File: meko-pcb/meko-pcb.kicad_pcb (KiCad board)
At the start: 4 copper layers, 37 x 69 mm, 165 parts, among them IC1 AS5600-ASOM, IC2 TCAL9538RSVR, IC3 LP5912-3.3DRVR, IC4 ES9218PQ, IC5 BQ27427YZFR, J1 GDEY0154D67, J2 MEM2090-00-145-00-A, J3 USB_C_Receptacle_USB2.0_16P, J4 SJ2-35954B-SMT-TR, M1 HD-EMB1204-SM, Q1 SS8050, Q2 SS8050, Q3 SS8050, Q4 Si1308EDL, SW1 SW_Push, SW2 SW_Push, SW3 SW_Push, SW4 SW_Push, SW5 SW_Push, SW6 SW_Push, SW7 SW_Push, U1 ESP32-PICO-MINI-02, U10 LP5907SNX-1.8/NOPB, U2 BQ24075RGT, U3 LP5907SNX-3.3/NOPB, U4 LP5907SNX-3.3/NOPB, U6 LP5907SNX-3.3/NOPB, U7 LP5907SNX-1.8/NOPB, U8 USBLC6-2SC6, U9 CP2102N-Axx-xQFN24, Y1 ECS-2520SMV-500-GP-TR

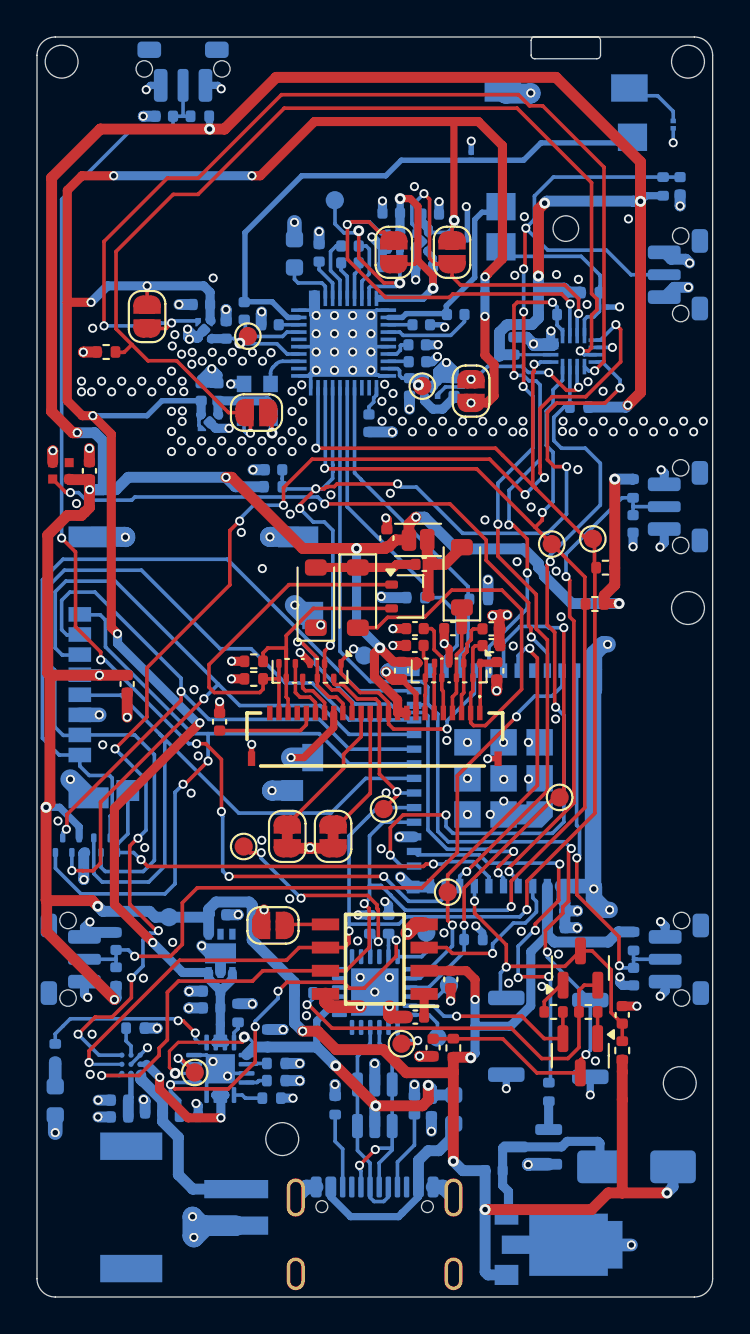
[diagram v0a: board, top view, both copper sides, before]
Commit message: removed seperate pcb file, you can undround the tracks easily
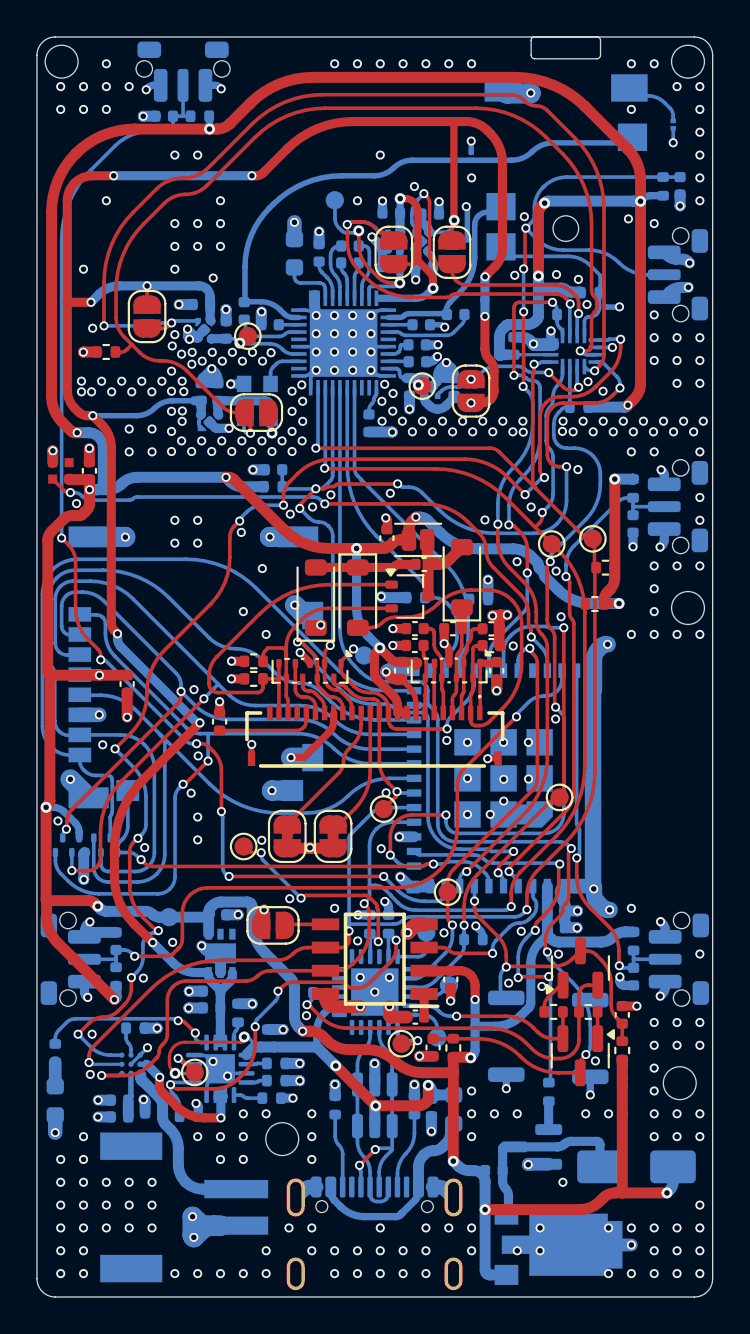
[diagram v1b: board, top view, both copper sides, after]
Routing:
- net +3V3: track 283.7 -> 278.5 mm
- net GND: track 192.5 -> 188.2 mm, vias 281 -> 455
- net /PWR_FUEL_GPOUT: track 71.0 -> 68.1 mm
- net REG-OUT: track 131.2 -> 128.3 mm
- net /I2C_SCL: track 88.6 -> 86.6 mm
- net /AUDIO_DATA_CLK/BOOT: track 60.3 -> 58.4 mm
- net /AUDIO_MLCK_EN: track 58.6 -> 56.8 mm
- net /BTN_VOL_UP: track 59.3 -> 57.9 mm
- net /MEM_DAT0: track 47.6 -> 46.2 mm
- net /PWR_EN3V3VCCA: track 55.8 -> 54.6 mm
- net /AUDIO_DISPL_RESETB: track 52.2 -> 51.2 mm
- net /I2C_SDA: track 89.4 -> 88.4 mm
- net /BTN_PWR: track 65.7 -> 64.7 mm
- net /MEM_DAT1: track 40.9 -> 39.9 mm
- net /MEM_CLK: track 35.5 -> 34.5 mm
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
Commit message: small changes, readme updates
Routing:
- net GND: vias 455 -> 540

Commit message: continued work om nrf53
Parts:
- removed C23, C25, C26: 4.7uF, Capacitor_SMD:C_0402_1005Metric
- removed C57, C58: 1uF, Capacitor_SMD:C_0402_1005Metric
- removed D14: LED, LED_SMD:LED_0603_1608Metric
- removed IC2: TCAL9538RSVR, TCAL9538RSVR:QFN40P180X260X55-16N
- removed IC5: BQ27427YZFR, BQ27427YZFR:BGA9C50P3X3_158X162X62
- removed Q1, Q2: SS8050, Package_TO_SOT_SMD:SOT-23
- removed R1, R14, R15, R16, R18, R2, R21, R22, R23, R24, R3, R31, R4, R5, R6, R7, R8: 10k, Resistor_SMD:R_0402_1005Metric
- removed R17: 47k, Resistor_SMD:R_0402_1005Metric
- removed R19, R32: 1.5k, Resistor_SMD:R_0402_1005Metric
- removed R20: 1.8k, Resistor_SMD:R_0402_1005Metric
- removed R30: 100k, Resistor_SMD:R_0402_1005Metric
- removed SW7: SW_Push, Button_Switch_SMD:SW_Push_SPST_NO_Alps_SKRK
- removed TP1, TP10, TP2, TP3, TP4, TP5, TP6, TP7: TestPoint, TestPoint:TestPoint_Pad_D1.0mm
- removed U8: USBLC6-2SC6, Package_TO_SOT_SMD:SOT-23-6
- removed U9: CP2102N-Axx-xQFN24, Package_DFN_QFN:QFN-24-1EP_4x4mm_P0.5mm_EP2.6x2.6mm
- added C31: 12pF, Capacitor_SMD:C_0402_1005Metric, F.Cu at (48.8, 71.0)
- added C32: 12pF, Capacitor_SMD:C_0402_1005Metric, F.Cu at (48.8, 73.0)
- added C35: 100nF, Capacitor_SMD:C_0402_1005Metric, F.Cu at (48.8, 75.0)
- added C37: 100nF, Capacitor_SMD:C_0402_1005Metric, F.Cu at (48.8, 77.0)
- added C39: 100nF, Capacitor_SMD:C_0402_1005Metric, F.Cu at (51.7, 67.1)
- added C59: 100nF, Capacitor_SMD:C_0402_1005Metric, F.Cu at (51.7, 71.0)
- added C62: 100nF, Capacitor_SMD:C_0402_1005Metric, F.Cu at (51.7, 77.0)
- added C63: 100nF, Capacitor_SMD:C_0402_1005Metric, F.Cu at (54.5, 67.1)
- added C64: 100nF, Capacitor_SMD:C_0402_1005Metric, F.Cu at (54.5, 69.1)
- added C65: 0.7pF, Capacitor_SMD:C_0402_1005Metric, F.Cu at (54.5, 71.0)
- added C66: N.C., Capacitor_SMD:C_0402_1005Metric, F.Cu at (54.5, 73.0)
- added C67: 2.2nF, Capacitor_SMD:C_0402_1005Metric, F.Cu at (54.5, 75.0)
- added C68: 1uF, Capacitor_SMD:C_0402_1005Metric, F.Cu at (54.5, 77.0)
- added C69: 1uF, Capacitor_SMD:C_0402_1005Metric, F.Cu at (57.4, 67.1)
- added C70: 100nF, Capacitor_SMD:C_0402_1005Metric, F.Cu at (57.4, 69.1)
- added C71: 4.7uF, Capacitor_SMD:C_0402_1005Metric, F.Cu at (57.4, 71.0)
- added C72: 4.7uF, Capacitor_SMD:C_0402_1005Metric, F.Cu at (57.4, 73.0)
- added Y2: 32MHz, Crystal:Crystal_SMD_2520-4Pin_2.5x2.0mm, F.Cu at (61.3, 61.5)
- added Y4: 32.768 kHz, Crystal:Crystal_SMD_3215-2Pin_3.2x1.5mm, F.Cu at (61.6, 57.8)
- C15: value 1uF -> 12pF; moved to F.Cu
- C40, C61, F1, R25, R26: moved to F.Cu
- C6: value 100nF -> 12pF
- C60: value 4.7uF -> 100nF; moved to F.Cu
- U1: value ESP32-PICO-MINI-02 -> nRF5340-QKxx; footprint PCM_Espressif:ESP32-PICO-MINI-02 -> Package_DFN_QFN:Nordic_AQFN-94-1EP_7x7mm_P0.4mm
- U2: value BQ24075RGT -> TP4056-42-ESOP8; footprint Package_DFN_QFN:VQFN-16-1EP_3x3mm_P0.5mm_EP1.6x1.6mm -> Package_SO:SOIC-8-1EP_3.9x4.9mm_P1.27mm_EP2.41x3.3mm_ThermalVias
- moved C15 59.4 mm to (48.8, 69.1), turned to 0 degrees
- moved C6 57.3 mm to (48.8, 67.1), turned to 0 degrees
- moved U1 54.6 mm to (51.7, 89.3), turned to 180 degrees
- moved C61 50.6 mm to (51.7, 75.0)
- moved C60 50.3 mm to (51.7, 73.0), turned to 0 degrees
- moved C40 44.8 mm to (51.7, 69.1), turned to 0 degrees
- moved F1 38.5 mm to (61.0, 64.8), turned to 0 degrees
- moved R26 34.0 mm to (65.0, 62.5), turned to 0 degrees
- moved R25 31.5 mm to (65.0, 60.5), turned to 0 degrees
- moved U2 18.9 mm to (64.8, 80.6), turned to -90 degrees
- moved J3 0.17 mm to (92.2, 88.2)
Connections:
- net /USB/CC1 renamed /CC1
- net /USB/CC2 renamed /CC2
- C15 pad 1: GND -> /XC1
- C15 pad 2: +3V3 -> GND
- C6 pad 1: /ESP_EN -> /XL2
- C60 pad 1: GND -> Net-(C35-Pad1)
- C60 pad 2: +3V3 -> GND
- C61 pad 1: +3V3 -> Net-(C35-Pad1)
- C7 pad 1: /AUDIO_DATA_CLK/BOOT -> unconnected-(C7-Pad1)
- J3 pad A6: /USB/D+ -> /D+
- J3 pad A7: /USB/D- -> /D-
- J3 pad B6: /USB/D+ -> /D+
- J3 pad B7: /USB/D- -> /D-
- U2 pad 1: /power/TS -> unconnected-(U2-TEMP-Pad1)
- U2 pad 2: /power/SRX -> unconnected-(U2-PROG-Pad2)
- U2 pad 3: /power/SRX -> unconnected-(U2-GND-Pad3)
- U2 pad 4: GND -> unconnected-(U2-V_{CC}-Pad4)
- U2 pad 5: /PWR_EN_USB -> unconnected-(U2-BAT-Pad5)
- U2 pad 6: +5V -> unconnected-(U2-~{STDBY}-Pad6)
- U2 pad 7: Net-(U2-~{PGOOD}) -> unconnected-(U2-~{CHRG}-Pad7)
- U2 pad 8: GND -> unconnected-(U2-CE-Pad8)
- U2 pad 9: Net-(U2-~{CHG}) -> unconnected-(U2-EPAD-Pad9)
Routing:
- net (no net): track 0.00 -> 300.5 mm, vias 0 -> 37
- net /PWR_FUEL_GPOUT: track 68.1 -> 0.00 mm, vias 10 -> 0
- net /EXP_~{INT}: track 41.9 -> 0.00 mm, vias 4 -> 0
- net /RXD: track 28.8 -> 0.00 mm, vias 2 -> 0
- net /EXP_~{RES}: track 26.9 -> 0.00 mm, vias 4 -> 0
- net /TXD: track 23.0 -> 0.00 mm, vias 2 -> 0
- net /PWR_EN_USB: track 22.8 -> 0.00 mm, vias 4 -> 0
- net /~{RST}: track 22.4 -> 0.00 mm, vias 1 -> 0
- net /USB/~{SUSP}: track 12.8 -> 0.00 mm, vias 3 -> 0
- net /USB/D+: track 12.5 -> 0.00 mm, vias 2 -> 0
- net /D+: track 0.00 -> 12.5 mm, vias 0 -> 2
- net /USB/D-: track 11.3 -> 0.00 mm
- net /D-: track 0.00 -> 11.3 mm
- net /~{DTR}: track 10.4 -> 0.00 mm, vias 1 -> 0
- net Net-(U2-~{CHG}): track 9.79 -> 0.00 mm, vias 2 -> 0
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
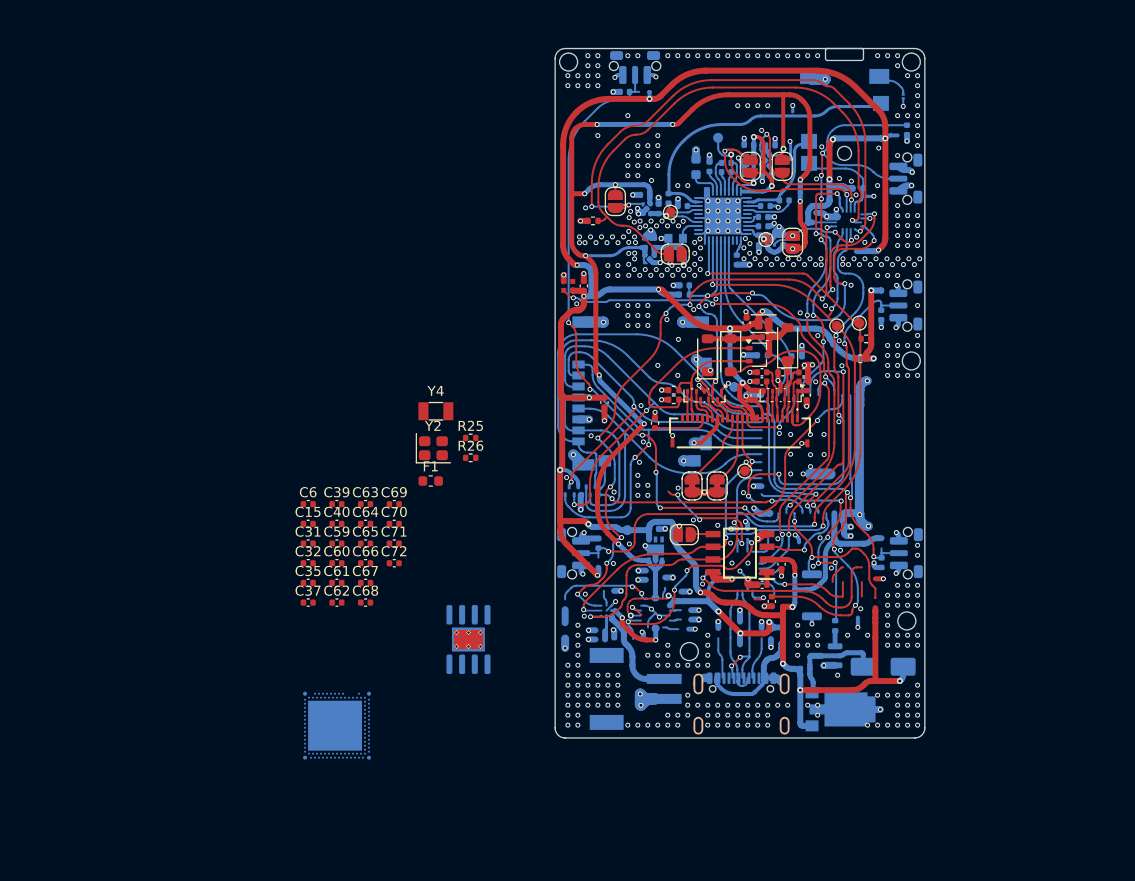
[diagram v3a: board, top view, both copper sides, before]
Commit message: added new ldos, made improvements to the schematic
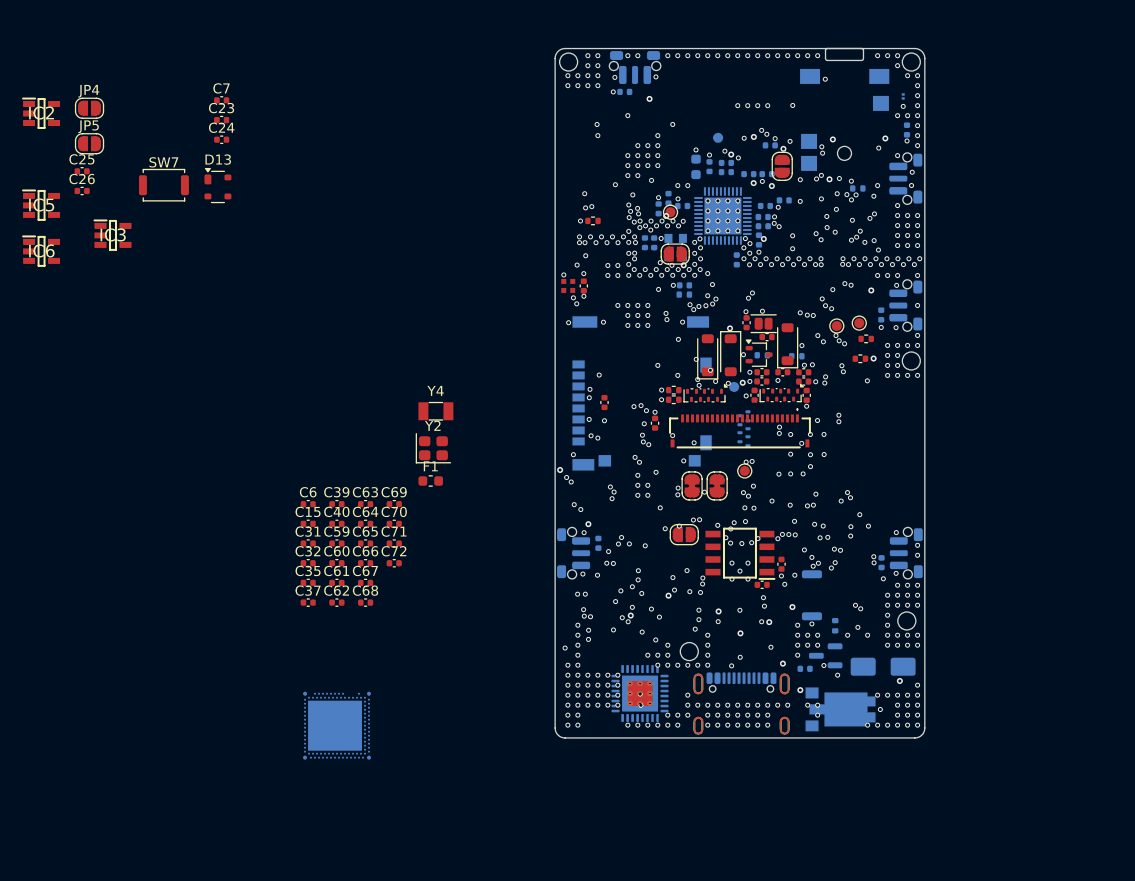
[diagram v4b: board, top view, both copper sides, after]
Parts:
- removed BT1: Battery_Cell, S2B-PH-SM4-TB_LF__SN_:JST_S2B-PH-SM4-TB_LF__SN_
- removed C29, C36, C38: 1uF, Capacitor_SMD:C_0402_1005Metric
- removed C33: 4.7uF, Capacitor_SMD:C_0402_1005Metric
- removed D10, D11, D12: D_TVS, CD0201-T2.0LC:CD0201T20LC
- removed JP10, JP6, JP8: SolderJumper_2_Open, Jumper:SolderJumper-2_P1.3mm_Open_RoundedPad1.0x1.5mm
- removed R25, R26: 5.1k, Resistor_SMD:R_0402_1005Metric
- removed TP17, TP18: TestPoint, TestPoint:TestPoint_Pad_D1.0mm
- removed U10, U7: LP5907SNX-1.8/NOPB, Package_SON:Texas_X2SON-4_1x1mm_P0.65mm
- removed U3, U4, U6: LP5907SNX-3.3/NOPB, Package_SON:Texas_X2SON-4_1x1mm_P0.65mm
- added C23: 10uF, Capacitor_SMD:C_0402_1005Metric, F.Cu at (40.1, 28.7)
- added C25: 1uF, Capacitor_SMD:C_0402_1005Metric, F.Cu at (26.2, 33.8)
- added C26: 1uF, Capacitor_SMD:C_0402_1005Metric, F.Cu at (26.2, 35.8)
- added D13: PRTR5V0U2X, Package_TO_SOT_SMD:SOT-143, F.Cu at (39.8, 35.4)
- added IC2: TPS7A2033PDBVR, TPS7A2018PDBVR:SOT95P280X145-5N, F.Cu at (22.1, 28.0)
- added IC5: TPS7A2018PDBVR, TPS7A2018PDBVR:SOT95P280X145-5N, F.Cu at (22.1, 37.2)
- added IC6: TPS7A2033PDBVR, TPS7A2018PDBVR:SOT95P280X145-5N, F.Cu at (22.1, 41.8)
- added JP4: SolderJumper_2_Open, Jumper:SolderJumper-2_P1.3mm_Open_RoundedPad1.0x1.5mm, F.Cu at (26.9, 27.5)
- added JP5: SolderJumper_2_Open, Jumper:SolderJumper-2_P1.3mm_Open_RoundedPad1.0x1.5mm, F.Cu at (26.9, 31.0)
- added SW7: SW_Push, Button_Switch_SMD:SW_Push_SPST_NO_Alps_SKRK, F.Cu at (34.4, 35.2)
- C24: moved to F.Cu
- C40: value 10uF -> 1uF
- C7: value 100nF -> 10uF
- IC3: value LP5912-3.3DRVR -> TPS7A2033PDBVR; footprint LP5912-3.3DRVR:SON65P200X200X80-7N -> TPS7A2018PDBVR:SOT95P280X145-5N; moved to F.Cu
- U2: value TP4056-42-ESOP8 -> nPM1300-QEXX; footprint Package_SO:SOIC-8-1EP_3.9x4.9mm_P1.27mm_EP2.41x3.3mm_ThermalVias -> Package_DFN_QFN:QFN-32-1EP_5x5mm_P0.5mm_EP3.6x3.6mm_ThermalVias
- moved C7 74.5 mm to (40.1, 26.7), turned to 0 degrees
- moved C24 63.7 mm to (40.1, 30.6)
- moved IC3 62.8 mm to (29.2, 40.2), turned to 0 degrees
- moved U2 18.0 mm to (82.0, 86.1), turned to 180 degrees
- moved D8 17.3 mm to (92.4, 59.6), turned to 180 degrees
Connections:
- C10 pad 1: +3V3 -> +HALL3V3
- C35 pad 1: Net-(C35-Pad1) -> +3V3
- C37 pad 1: Net-(C35-Pad1) -> +3V3
- C39 pad 1: Net-(C35-Pad1) -> +3V3
- C40 pad 1: +5V -> (no net)
- C49 pad 1: +3V3AVDD -> +3V3
- C59 pad 1: Net-(C35-Pad1) -> +3V3
- C60 pad 1: Net-(C35-Pad1) -> +3V3
- C61 pad 1: Net-(C35-Pad1) -> +3V3
- C62 pad 1: Net-(C35-Pad1) -> +3V3
- C63 pad 1: Net-(C35-Pad1) -> +3V3
- C7 pad 1: unconnected-(C7-Pad1) -> Net-(U2-VOUT1)
- C71 pad 1: Net-(U1-VBUS) -> VBUSOUT
- F1 pad 1: +5V -> VBUSIN
- IC1 pad 2: +3V3 -> +HALL3V3
- IC3 pad 1: +3V3 -> REG-OUT
- IC3 pad 2: unconnected-(IC3-NC-Pad2) -> GND
- IC3 pad 3: unconnected-(IC3-PG-Pad3) -> /PWR_EN3V3AVCC
- IC3 pad 4: REG-OUT -> unconnected-(IC3-N/C-Pad4)
- IC3 pad 5: GND -> +3V3AVCC
- IC4 pad 29: +3V3AVDD -> +3V3
- J3 pad A5: /CC2 -> /CC1
- J3 pad B5: /CC1 -> /CC2
- U1 pad A19: Net-(C35-Pad1) -> +3V3
- U1 pad A5: Net-(U1-VBUS) -> VBUSOUT
- U1 pad AC1: Net-(C35-Pad1) -> +3V3
- U1 pad AG1: Net-(C35-Pad1) -> +3V3
- U1 pad AJ31: Net-(C35-Pad1) -> +3V3
- U1 pad AL11: Net-(C35-Pad1) -> +3V3
- U1 pad AL17: Net-(C35-Pad1) -> +3V3
- U1 pad AL25: Net-(C35-Pad1) -> +3V3
- U1 pad AL3: Net-(C35-Pad1) -> +3V3
- U1 pad AL7: Net-(C35-Pad1) -> +3V3
- U1 pad B28: Net-(C35-Pad1) -> +3V3
- U1 pad B8: Net-(C35-Pad1) -> +3V3
- U1 pad C1: Net-(C35-Pad1) -> +3V3
- U1 pad E1: unconnected-(U1-VDDH-PadE1) -> +3V3
- U1 pad E31: Net-(C35-Pad1) -> +3V3
- U1 pad EP: unconnected-(U1-VSS-PadEP) -> GND
- U1 pad J1: unconnected-(U1-DCCH-PadJ1) -> Net-(U1-DCCH)
- U1 pad L1: Net-(C35-Pad1) -> +3V3
- U1 pad N31: Net-(C35-Pad1) -> +3V3
- U1 pad U1: Net-(C35-Pad1) -> +3V3
- U2 pad 1: unconnected-(U2-TEMP-Pad1) -> Net-(U2-VOUT1)
- U2 pad 2: unconnected-(U2-PROG-Pad2) -> GND
- U2 pad 3: unconnected-(U2-GND-Pad3) -> Net-(U2-SW1)
- U2 pad 5: unconnected-(U2-BAT-Pad5) -> Net-(U2-SW2)
- U2 pad 6: unconnected-(U2-~{STDBY}-Pad6) -> GND
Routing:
- net (no net): track 300.5 -> 0.00 mm, vias 37 -> 45
- net +3V3: track 278.5 -> 0.00 mm, vias 23 -> 24
- net GND: track 188.2 -> 0.00 mm
- net REG-OUT: track 128.3 -> 0.00 mm
- net /I2C_SDA: track 88.4 -> 0.00 mm
- net /I2C_SCL: track 86.6 -> 0.00 mm
- net /BTN_PWR: track 64.7 -> 0.00 mm
- net /AUDIO_DATA_CLK/BOOT: track 58.4 -> 0.00 mm
- net /BTN_VOL_UP: track 57.9 -> 0.00 mm
- net /AUDIO_MLCK_EN: track 56.8 -> 0.00 mm
- net /PWR_EN3V3VCCA: track 54.6 -> 0.00 mm
- net /AUDIO_DISPL_RESETB: track 51.2 -> 0.00 mm
- net /MEM_DAT0: track 46.2 -> 0.00 mm
- net /MEM_CMD: track 42.2 -> 0.00 mm
- net /MEM_DAT1: track 39.9 -> 0.00 mm
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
